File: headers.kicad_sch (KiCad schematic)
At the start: 0 parts

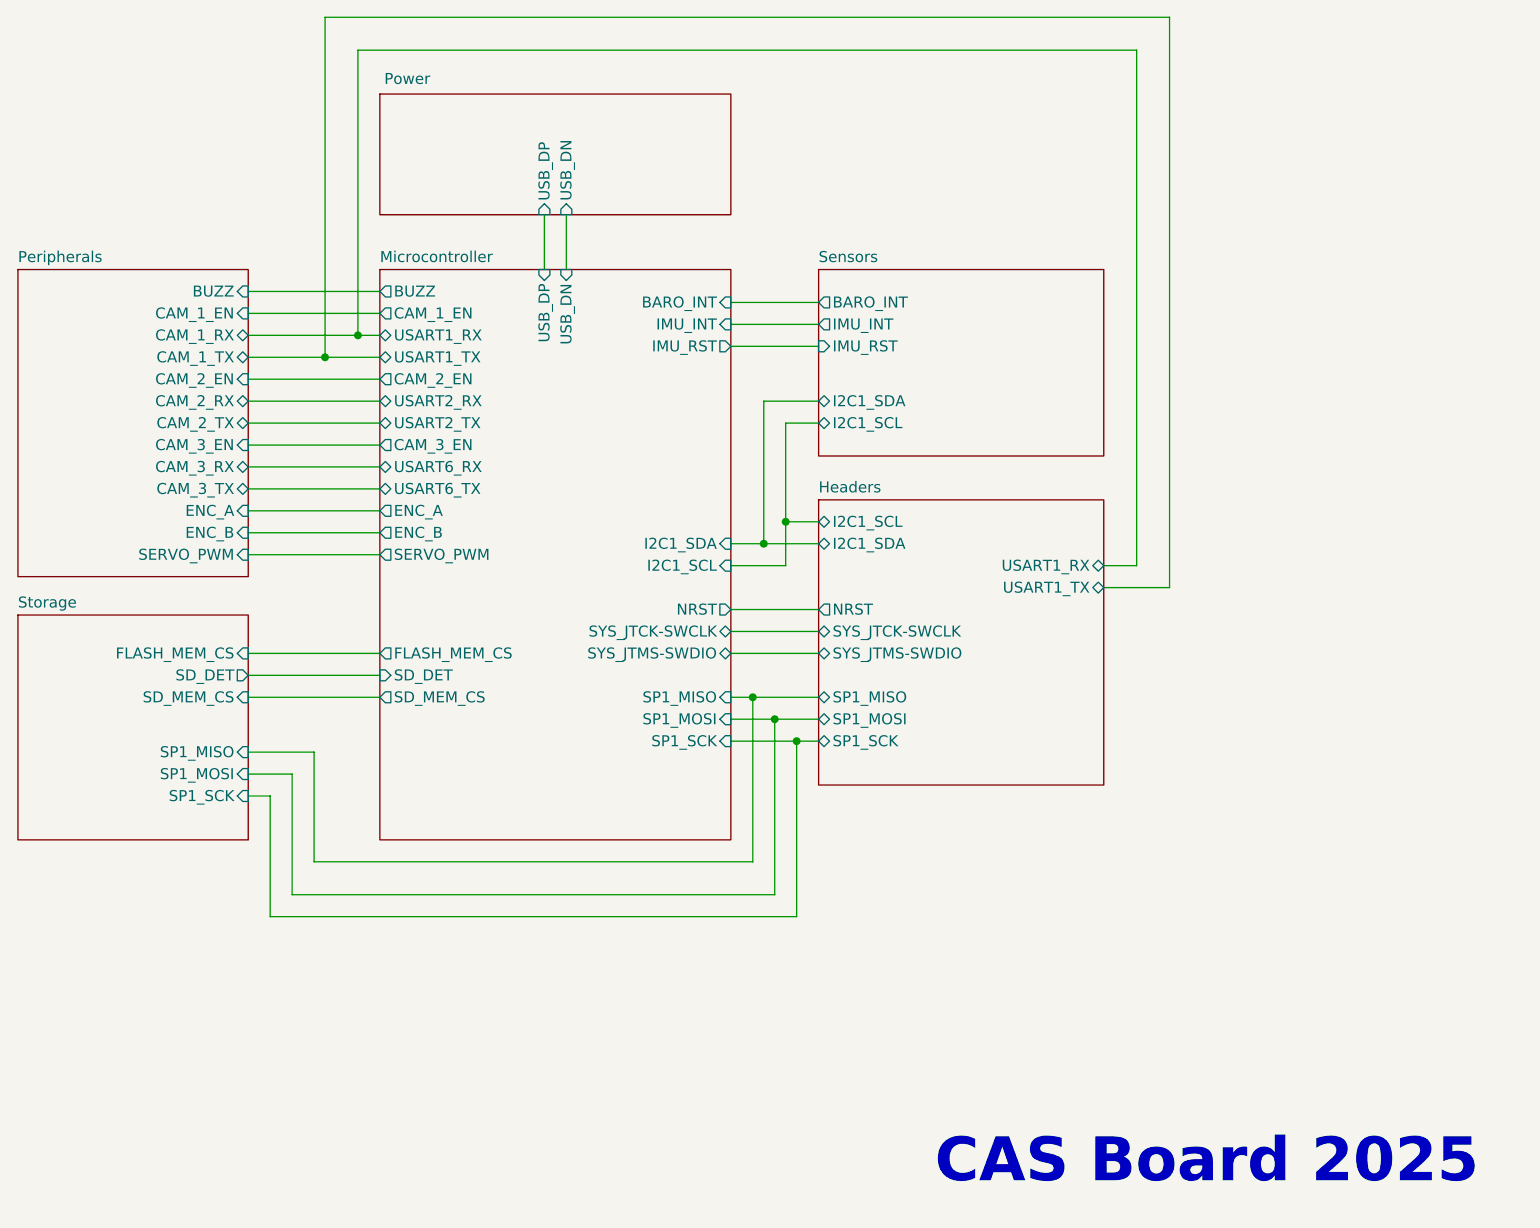
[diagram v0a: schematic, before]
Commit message: Broke headers into own heiarchicial sheet
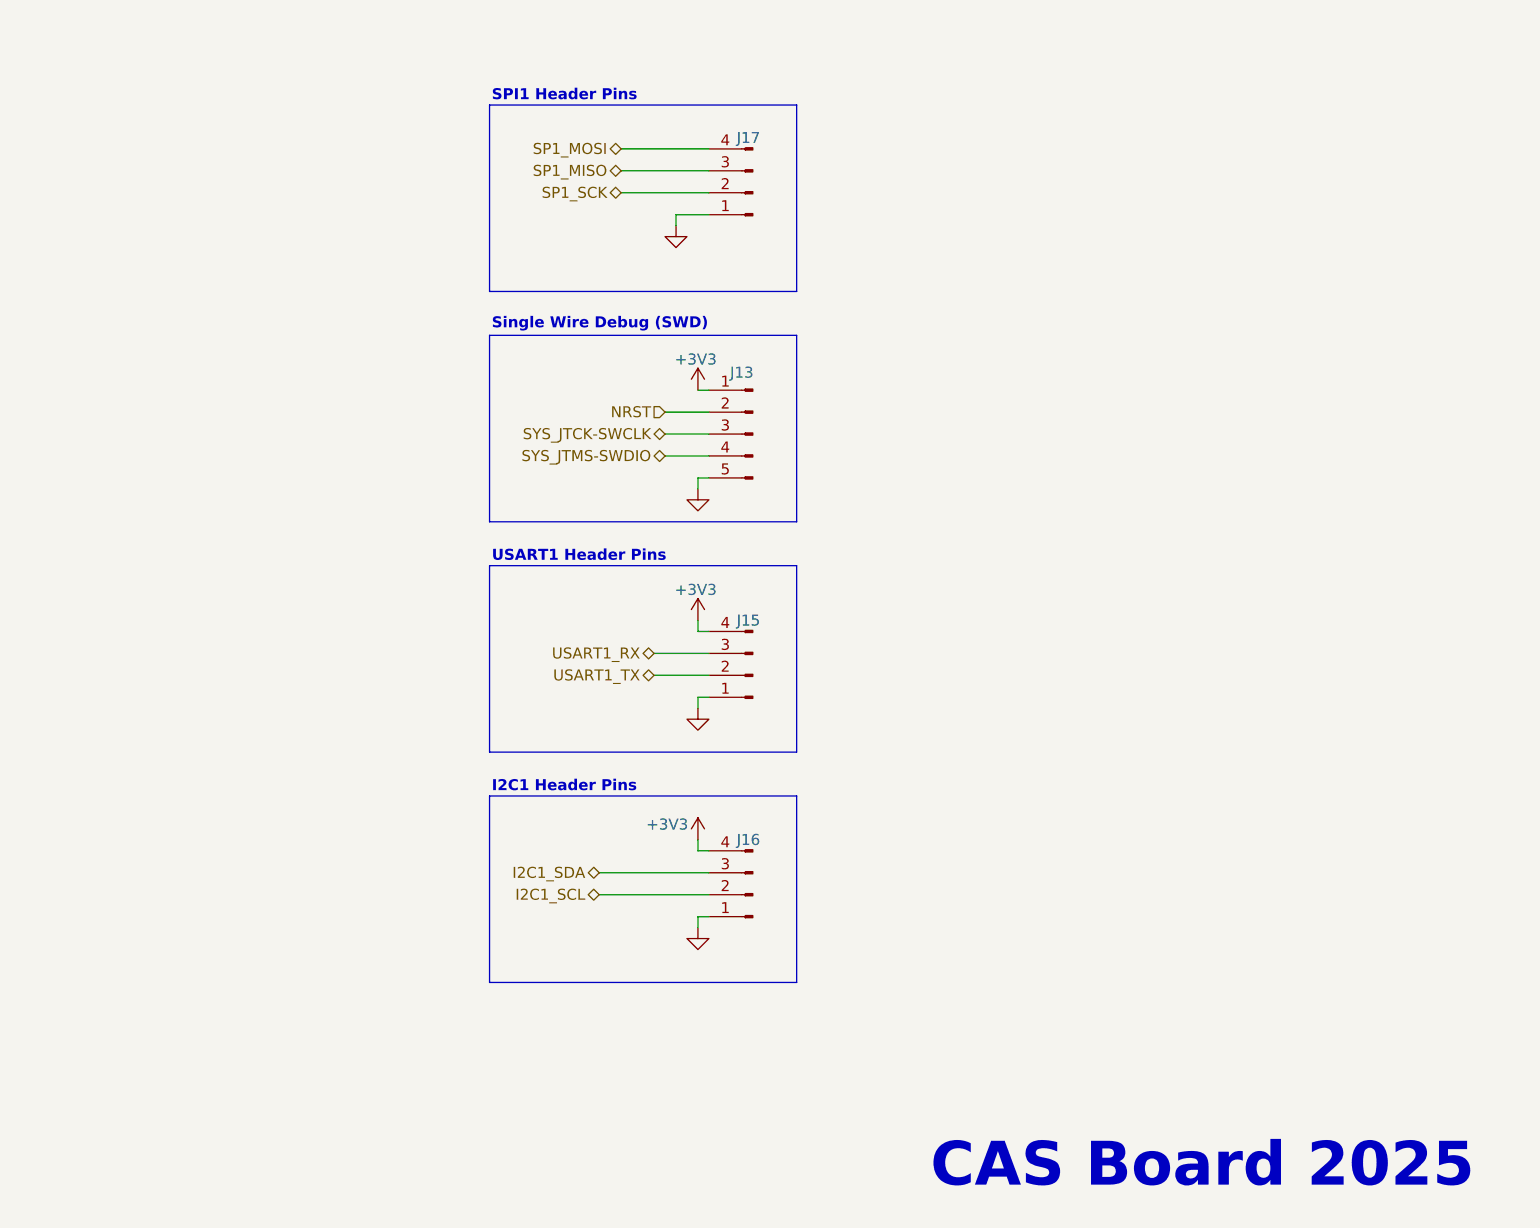
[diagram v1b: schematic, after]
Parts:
- added J13: SWD Header, Connector_PinHeader_2.54mm:PinHeader_1x05_P2.54mm_Vertical, symbol Connector:Conn_01x05_Pin
- added J15: USART1 Header, Connector_PinHeader_2.54mm:PinHeader_1x04_P2.54mm_Vertical, symbol Connector:Conn_01x04_Pin
- added J16: I2C1 Header, Connector_PinHeader_2.54mm:PinHeader_1x04_P2.54mm_Vertical, symbol Connector:Conn_01x04_Pin
- added J17: SPI Header, Connector_PinHeader_2.54mm:PinHeader_1x04_P2.54mm_Vertical, symbol Connector:Conn_01x04_Pin
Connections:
- new net +3V3: J13.1 (Pin_1), J15.4 (Pin_4), J16.4 (Pin_4)
- new net GND: J13.5 (Pin_5), J15.1 (Pin_1), J16.1 (Pin_1), J17.1 (Pin_1)
- new net I2C1_SCL: J16.2 (Pin_2)
- new net I2C1_SDA: J16.3 (Pin_3)
- new net NRST: J13.2 (Pin_2)
- new net SP1_MISO: J17.3 (Pin_3)
- new net SP1_MOSI: J17.4 (Pin_4)
- new net SP1_SCK: J17.2 (Pin_2)
- new net SYS_JTCK-SWCLK: J13.3 (Pin_3)
- new net SYS_JTMS-SWDIO: J13.4 (Pin_4)
- new net USART1_RX: J15.3 (Pin_3)
- new net USART1_TX: J15.2 (Pin_2)
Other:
- removed sheet Headers
- removed sheet Microcontroller
- removed sheet Peripherals
- removed sheet Power
- removed sheet Sensors
- removed sheet Storage
- note added: "I2C1 Header Pins"
- note added: "SPI1 Header Pins"
- note added: "Single Wire Debug (SWD)"
- note added: "USART1 Header Pins"
- company: Lulu Systems -> (none)
- title: Simpler Flight v2 -> (none)

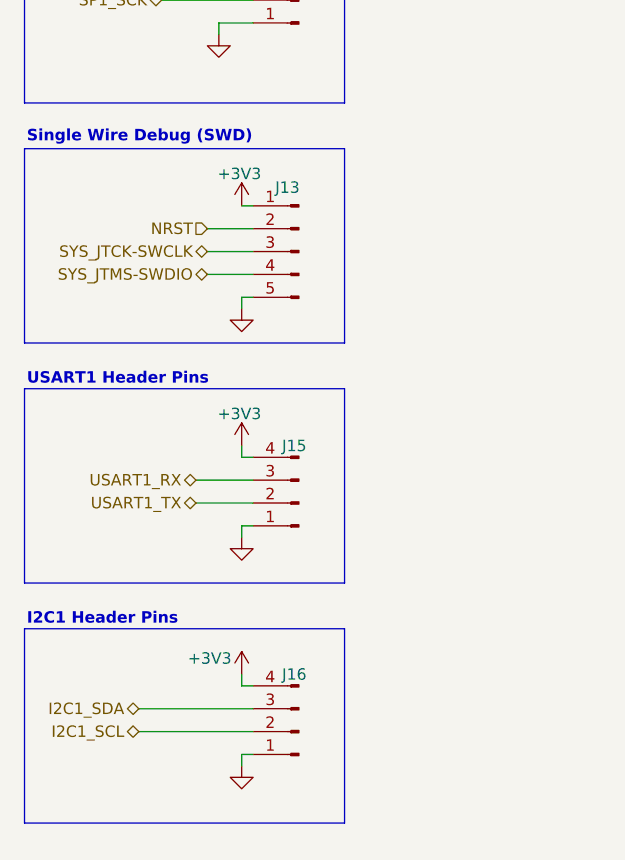
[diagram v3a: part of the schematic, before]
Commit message: Initial layout for PCB components, updated README with images. Removed some test points and headers from final layout. Pending addition of buzzer. Pending additional power testing and pending routing.
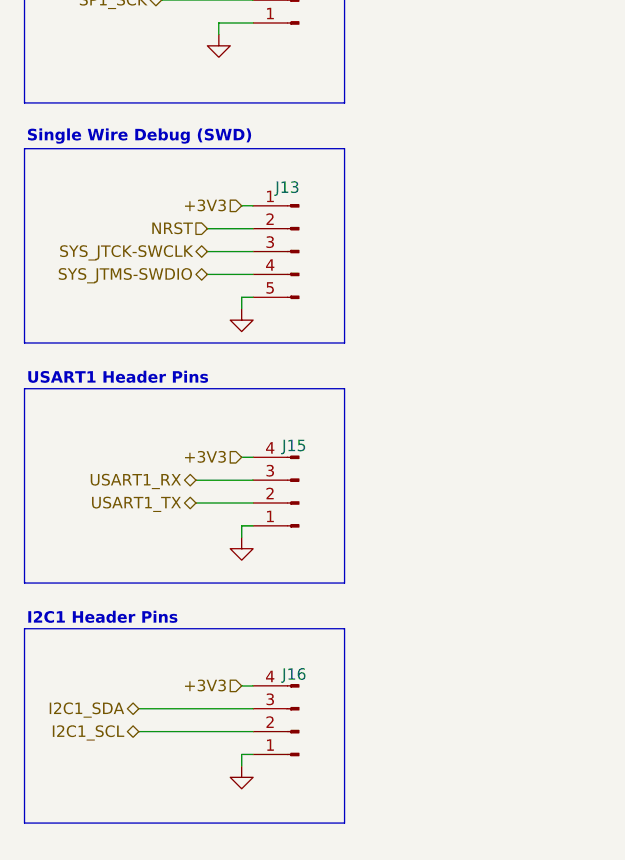
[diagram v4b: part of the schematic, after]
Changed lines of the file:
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@@
 	(wire
 		(pts
-			(xy 151.13 111.76) (xy 151.13 110.49)
-		)
-		(stroke
-			(width 0)
-			(type default)
-		)
-	)
-	(wire
-		(pts
 			(xy 151.13 93.98) (xy 152.4 93.98)
 		)
@@
 		)
 	)
-	(wire
-		(pts
-			(xy 151.13 137.16) (xy 151.13 135.89)
-		)
-		(stroke
-			(width 0)
-			(type default)
-		)
-	)
 	(polyline
 		(pts
@@
 		)
 	)
+	(hierarchical_label "+3V3"
+		(shape input)
+		(at 151.13 111.76 180)
+		(effects
+			(font
+				(size 1.27 1.27)
+			)
+			(justify right)
+		)
+	)
 	(hierarchical_label "SYS_JTCK-SWCLK"
 		(shape bidirectional)
@@
 		)
 	)
+	(hierarchical_label "+3V3"
+		(shape input)
+		(at 151.13 137.16 180)
+		(effects
+			(font
+				(size 1.27 1.27)
+			)
+			(justify right)
+		)
+	)
 	(hierarchical_label "I2C1_SDA"
 		(shape bidirectional)
@@
 		)
 	)
+	(hierarchical_label "+3V3"
+		(shape input)
+		(at 151.13 83.82 180)
+		(effects
+			(font
+				(size 1.27 1.27)
+			)
+			(justify right)
+		)
+	)
 	(hierarchical_label "USART1_RX"
 		(shape bidirectional)
@@
 	)
 	(symbol
-		(lib_id "power:+3V3")
-		(at 151.13 83.82 0)
-		(unit 1)
-		(exclude_from_sim no)
-		(in_bom yes)
-		(on_board yes)
-		(dnp no)
-		(property "Reference" "#PWR061"
-			(at 151.13 87.63 0)
-			(effects
-				(font
-					(size 1.27 1.27)
-				)
-				(hide yes)
-			)
-		)
-		(property "Value" "+3V3"
-			(at 150.876 80.264 0)
-			(effects
-				(font
-					(size 1.27 1.27)
-				)
-			)
-		)
-		(property "Footprint" ""
-			(at 151.13 83.82 0)
-			(effects
-				(font
-					(size 1.27 1.27)
-				)
-				(hide yes)
-			)
-		)
-		(property "Datasheet" ""
-			(at 151.13 83.82 0)
-			(effects
-				(font
-					(size 1.27 1.27)
-				)
-				(hide yes)
-			)
-		)
-		(property "Description" "Power symbol creates a global label with name \"+3V3\""
-			(at 151.13 83.82 0)
-			(effects
-				(font
-					(size 1.27 1.27)
-				)
-				(hide yes)
-			)
-		)
-		(pin "1"
-		)
-		(instances
-			(project "SimplerFlight_v2"
-				(path "/05521696-5bcb-4d0e-9e87-bbc993e58ce4/a742b009-1ff6-4992-9a6f-d7817eac5585"
-					(reference "#PWR061")
-					(unit 1)
-				)
-			)
-		)
-	)
-	(symbol
-		(lib_id "power:+3V3")
-		(at 151.13 135.89 0)
-		(unit 1)
-		(exclude_from_sim no)
-		(in_bom yes)
-		(on_board yes)
-		(dnp no)
-		(property "Reference" "#PWR065"
-			(at 151.13 139.7 0)
-			(effects
-				(font
-					(size 1.27 1.27)
-				)
-				(hide yes)
-			)
-		)
-		(property "Value" "+3V3"
-			(at 147.574 134.112 0)
-			(effects
-				(font
-					(size 1.27 1.27)
-				)
-			)
-		)
-		(property "Footprint" ""
-			(at 151.13 135.89 0)
-			(effects
-				(font
-					(size 1.27 1.27)
-				)
-				(hide yes)
-			)
-		)
-		(property "Datasheet" ""
-			(at 151.13 135.89 0)
-			(effects
-				(font
-					(size 1.27 1.27)
-				)
-				(hide yes)
-			)
-		)
-		(property "Description" "Power symbol creates a global label with name \"+3V3\""
-			(at 151.13 135.89 0)
-			(effects
-				(font
-					(size 1.27 1.27)
-				)
-				(hide yes)
-			)
-		)
-		(pin "1"
-		)
-		(instances
-			(project "SimplerFlight_v2"
-				(path "/05521696-5bcb-4d0e-9e87-bbc993e58ce4/a742b009-1ff6-4992-9a6f-d7817eac5585"
-					(reference "#PWR065")
-					(unit 1)
-				)
-			)
-		)
-	)
-	(symbol
 		(lib_id "power:GND")
 		(at 151.13 146.05 0)
@@
 					(unit 1)
 				)
-			)
-		)
-	)
-	(symbol
-		(lib_id "power:+3V3")
-		(at 151.13 110.49 0)
-		(unit 1)
-		(exclude_from_sim no)
-		(in_bom yes)
-		(on_board yes)
-		(dnp no)
-		(property "Reference" "#PWR063"
-			(at 151.13 114.3 0)
-			(effects
-				(font
-					(size 1.27 1.27)
-				)
-				(hide yes)
-			)
-		)
-		(property "Value" "+3V3"
-			(at 150.876 106.934 0)
-			(effects
-				(font
-					(size 1.27 1.27)
-				)
-			)
-		)
-		(property "Footprint" ""
-			(at 151.13 110.49 0)
-			(effects
-				(font
-					(size 1.27 1.27)
-				)
-				(hide yes)
-			)
-		)
-		(property "Datasheet" ""
-			(at 151.13 110.49 0)
-			(effects
-				(font
-					(size 1.27 1.27)
-				)
-				(hide yes)
-			)
-		)
-		(property "Description" "Power symbol creates a global label with name \"+3V3\""
-			(at 151.13 110.49 0)
-			(effects
-				(font
-					(size 1.27 1.27)
-				)
-				(hide yes)
-			)
-		)
-		(pin "1"
-		)
-		(instances
-			(project "SimplerFlight_v2"
-				(path "/05521696-5bcb-4d0e-9e87-bbc993e58ce4/a742b009-1ff6-4992-9a6f-d7817eac5585"
-					(reference "#PWR063")
-					(unit 1)
-				)

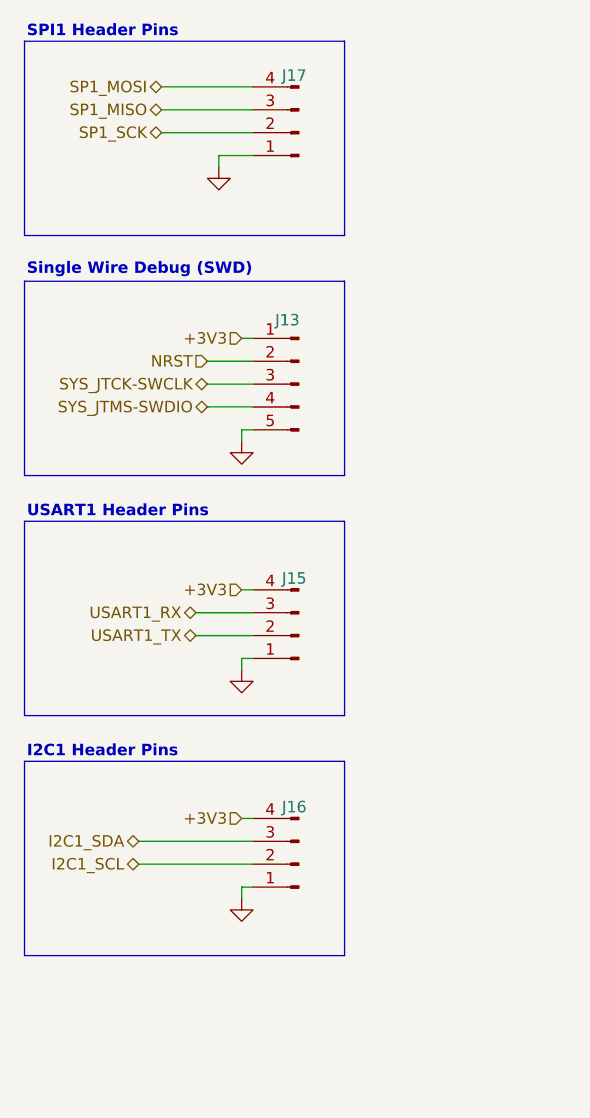
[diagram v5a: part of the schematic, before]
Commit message: Removed uncvessary test points and headerrs. Added missing values. Update images of schematics
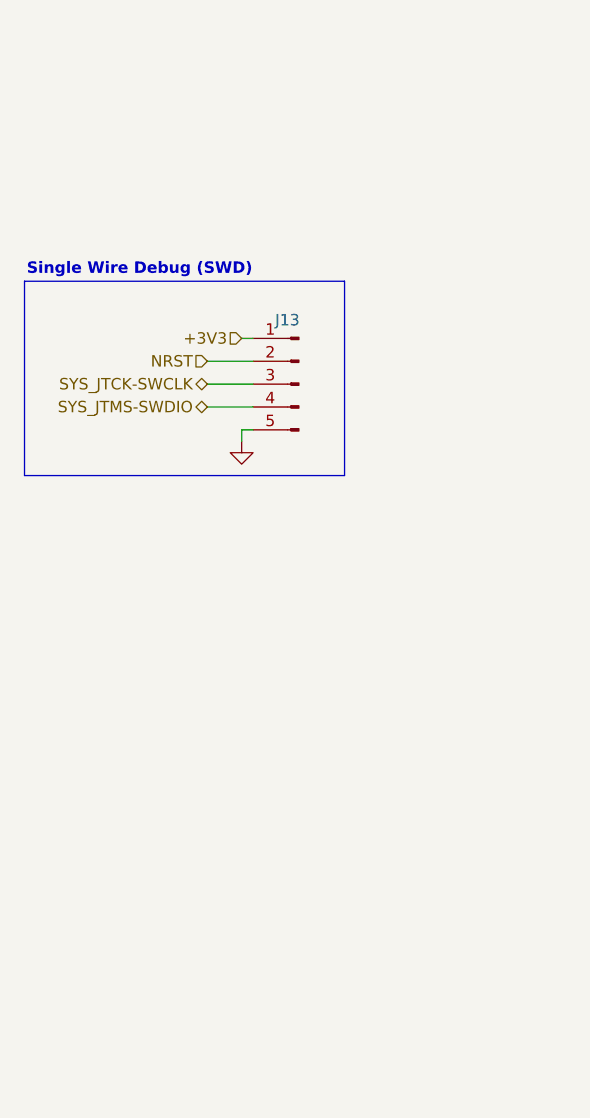
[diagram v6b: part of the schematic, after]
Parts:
- removed J15: USART1 Header, Connector_PinHeader_2.54mm:PinHeader_1x04_P2.54mm_Vertical, symbol Connector:Conn_01x04_Pin
- removed J16: I2C1 Header, Connector_PinHeader_2.54mm:PinHeader_1x04_P2.54mm_Vertical, symbol Connector:Conn_01x04_Pin
- removed J17: SPI Header, Connector_PinHeader_2.54mm:PinHeader_1x04_P2.54mm_Vertical, symbol Connector:Conn_01x04_Pin
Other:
- note removed: "I2C1 Header Pins"
- note removed: "SPI1 Header Pins"
- note removed: "USART1 Header Pins"
